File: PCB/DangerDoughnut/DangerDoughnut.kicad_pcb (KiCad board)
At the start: 4 copper layers, 50 x 37 mm, 85 parts, among them J1 Conn_01x02_Pin, J2 Conn_01x02_Pin, J3 Conn_01x02_Pin, J4 Conn_01x04_Pin, J6 USB_C_Receptacle_USB2.0_16P, U1 MMC5983MA, U10 ESP32-S3, U2 H3LIS331DLTR, U3 H3LIS331DLTR, U4 W25X20CLZP, U6 L5973D, U7 MIC5219-3.3YM5, U8 ESP8285H16, U9 SX1280IMLTRT, Y1 40MHz, Y2 52MHz, Y3 26MHz

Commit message: verified elsr
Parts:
- removed the C16 at (92.8, 70.2)
- removed the C17 at (88.8, 70.2)
- removed FL2: 2450FM07D0034T, Danger_Doughnut_Lib:FIL_2450FM07D0034T
- added C29: 100uF, Capacitor_THT:CP_Radial_D6.3mm_P2.50mm, B.Cu at (109.2, 59.5)
- added D6: Green LED, LED_SMD:LED_0805_2012Metric, F.Cu at (78.5, 64.8)
- added R20: 30, Resistor_SMD:R_0402_1005Metric, F.Cu at (78.5, 62.8)
- added R21: 100, Resistor_SMD:R_0402_1005Metric, F.Cu at (84.8, 56.8)
- added R22: 100, Resistor_SMD:R_0402_1005Metric, F.Cu at (86.6, 58.8)
- C1, C11, C14, C16, C17, C2, C20, C21, C22, C23, C25, C26, C27, C28, C3, C30, C32, C33, C6, C7, C9: footprint Capacitor_SMD:C_0603_1608Metric_Pad1.08x0.95mm_HandSolder -> Capacitor_SMD:C_0402_1005Metric
- C8: footprint Capacitor_SMD:CP_Elec_6.3x7.7 -> Capacitor_THT:CP_Radial_D6.3mm_P2.50mm
- D2: footprint Diode_SMD:D_SOD-882D -> Diode_SMD:D_0805_2012Metric
- D3: footprint Diode_SMD:D_SOD-882D -> Capacitor_SMD:C_0805_2012Metric
- R1, R10, R11, R12, R13, R14, R15, R16, R17, R18, R19, R2, R3, R4, R5, R6, R7, R8, R9: footprint Resistor_SMD:R_0603_1608Metric_Pad0.98x0.95mm_HandSolder -> Resistor_SMD:R_0402_1005Metric
- moved R16 4.56 mm to (100.0, 61.0), turned to -90 degrees
- moved C24 2.74 mm to (102.2, 70.0), turned to -90 degrees
- moved C23 2.25 mm to (100.5, 70.2)
- moved R12 2.00 mm to (99.0, 70.2)
- moved R17 1.68 mm to (101.8, 63.5)
- moved C26 1.66 mm to (101.8, 65.0)
- moved Y2 1.52 mm to (89.2, 70.5)
- moved C8 1.50 mm to (104.0, 66.5), turned to 180 degrees
- moved C15 1.35 mm to (97.8, 70.2)
- moved C5 1.35 mm to (93.8, 70.2)
- moved Y3 1.35 mm to (95.8, 70.2)
- moved D2 1.25 mm to (101.8, 45.5)
- moved U8 1.25 mm to (97.0, 65.5)
- moved D5 1.06 mm to (102.0, 61.0)
- moved kibuzzard-668D7854 1.06 mm to (106.0, 61.0)
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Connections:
- ANT2 pad 2: Net-(ANT2-FEED) -> unconnected-(ANT2-FEED-Pad2)
- J4 pad 1: GND -> Net-(J4-Pin_1)
- J4 pad 2: +5V -> Net-(J4-Pin_2)
- J4 pad 3: unconnected-(J4-Pin_3-Pad3) -> +5V
- J4 pad 4: unconnected-(J4-Pin_4-Pad4) -> GND
- U10 pad 1: Net-(U10-LNA_IN) -> unconnected-(U10-LNA_IN-Pad1)

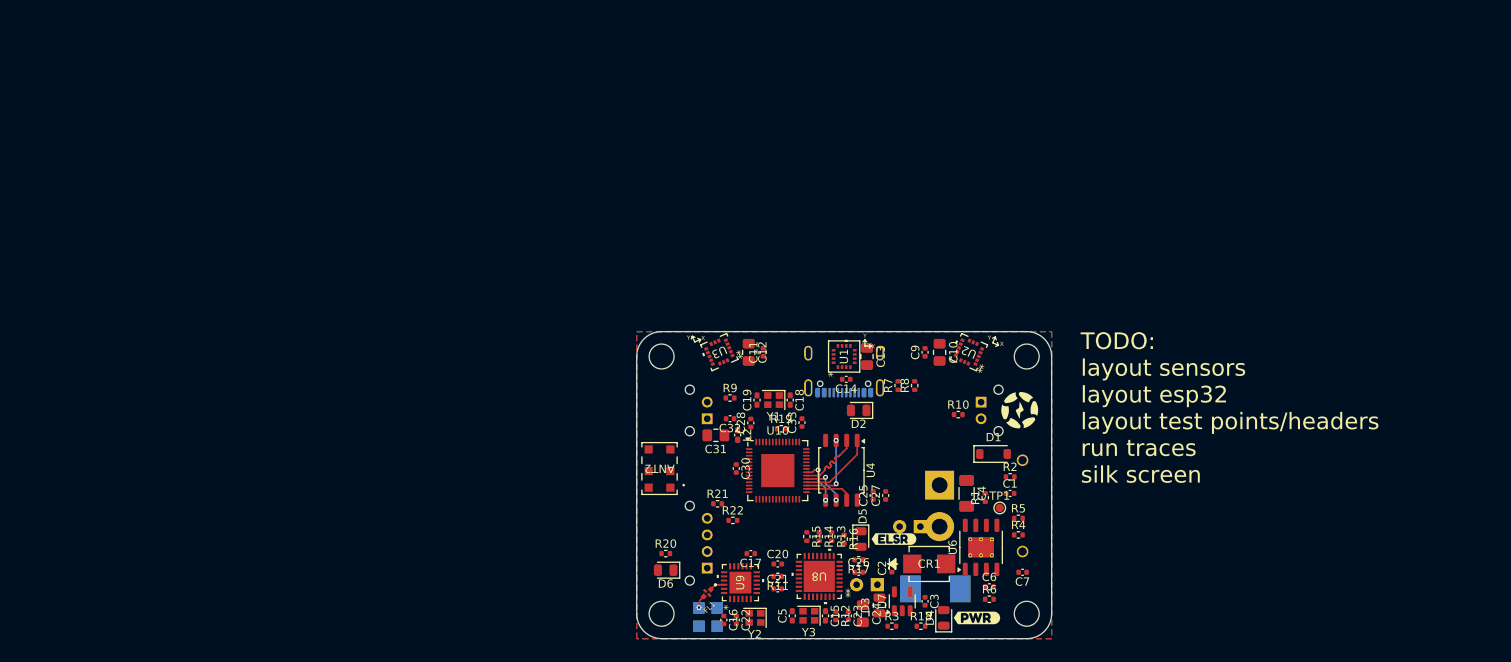
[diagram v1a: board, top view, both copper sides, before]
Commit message: updated schematic power layout done
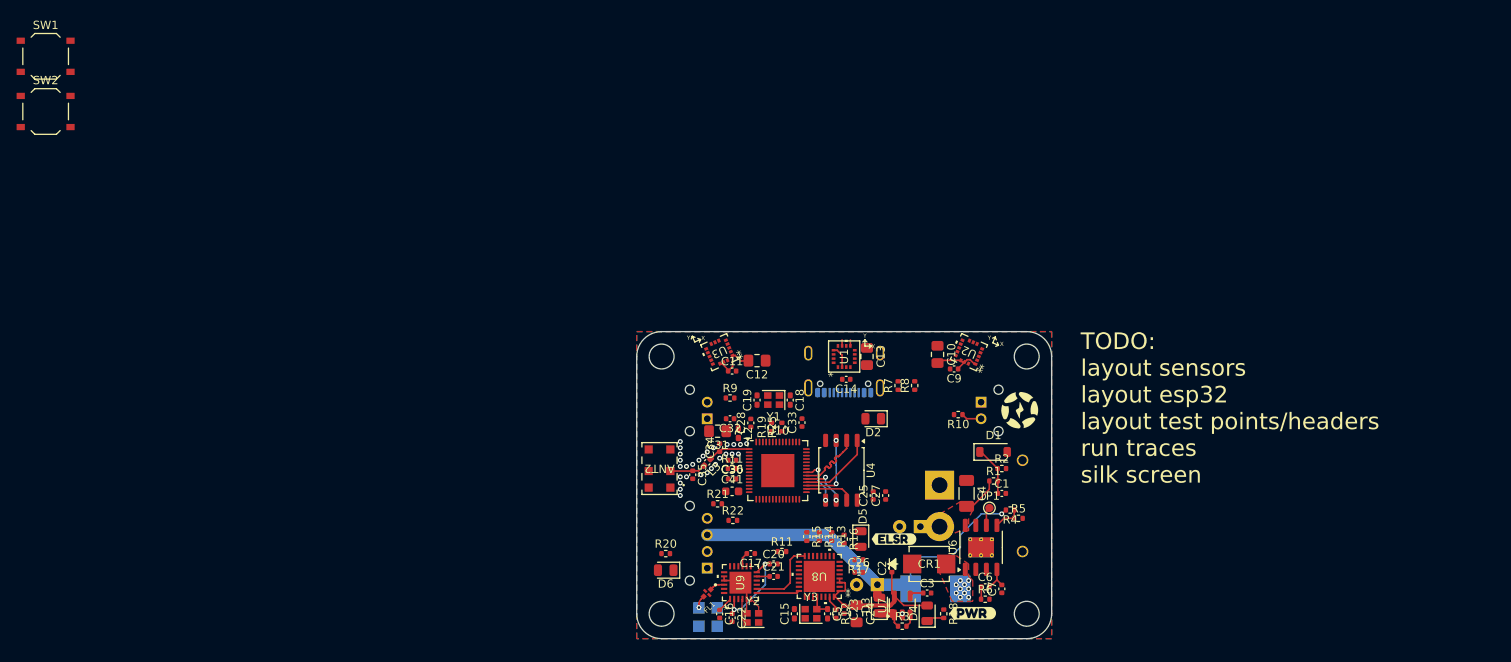
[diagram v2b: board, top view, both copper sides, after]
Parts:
- added C34: 1.8pF, Capacitor_SMD:C_0402_1005Metric, F.Cu at (85.0, 50.0)
- added C35: 1.2pF, Capacitor_SMD:C_0402_1005Metric, F.Cu at (81.8, 53.2)
- added C36: 1uF, Capacitor_SMD:C_0402_1005Metric, F.Cu at (86.5, 53.8)
- added C41: 100nF, Capacitor_SMD:C_0603_1608Metric, F.Cu at (86.5, 55.2)
- added L3: 3nH, Inductor_SMD:L_0402_1005Metric_Pad0.77x0.64mm_HandSolder, F.Cu at (83.5, 51.8)
- added R11: 10K, Resistor_SMD:R_0402_1005Metric, F.Cu at (86.5, 52.5)
- added R25: 510, Resistor_SMD:R_0402_1005Metric, F.Cu at (92.5, 47.5)
- added SW1: SW_Push, Button_Switch_SMD:SW_Push_1P1T_XKB_TS-1187A, F.Cu at (3.77, 2.83)
- added SW2: SW_Push, Button_Switch_SMD:SW_Push_1P1T_XKB_TS-1187A, F.Cu at (3.77, 9.47)
- D3: footprint Capacitor_SMD:C_0805_2012Metric -> Diode_SMD:D_0805_2012Metric
- R17, R18: value 2.2K -> 3.3k
- moved C11 4.37 mm to (86.5, 40.8), turned to 0 degrees
- moved C5 4.26 mm to (98.0, 70.0), turned to -90 degrees
- moved C9 4.03 mm to (113.2, 40.5), turned to 180 degrees
- moved C15 3.76 mm to (94.0, 70.0), turned to 90 degrees
- moved C7 3.20 mm to (119.0, 67.0), turned to 90 degrees
- moved R4 3.16 mm to (120.0, 57.5), turned to 180 degrees
- moved R18 3.13 mm to (112.0, 70.0), turned to -90 degrees
- moved R11 3.04 mm to (92.5, 62.5), turned to 0 degrees
- moved R1 2.24 mm to (118.0, 54.0), turned to 0 degrees
- moved D4 2.08 mm to (110.0, 69.9)
- moved D2 2.02 mm to (103.5, 46.5)
- moved C21 1.58 mm to (91.5, 65.5)
- moved C12 1.41 mm to (89.5, 39.5), turned to 180 degrees
- moved R2 1.41 mm to (119.0, 52.5)
- moved R3 1.25 mm to (107.0, 71.5)
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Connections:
- net Net-(U6-OUT) renamed /DCDC_OUT
- ANT2 pad 2: unconnected-(ANT2-FEED-Pad2) -> Net-(ANT2-FEED)
- C21 pad 1: Net-(U9-VBAT_IO) -> +3.3V
- U1 pad 15: unconnected-(U1-INT-Pad15) -> MAG_INT
- U10 pad 1: unconnected-(U10-LNA_IN-Pad1) -> Net-(U10-LNA_IN)
- U10 pad 10: unconnected-(U10-GPIO5-Pad10) -> Mag_CS
- U10 pad 11: unconnected-(U10-GPIO6-Pad11) -> Accel1_CS
- U10 pad 12: unconnected-(U10-GPIO7-Pad12) -> Accel2_CS
- U10 pad 16: unconnected-(U10-GPIO11-Pad16) -> LED_BOTTOM
- U10 pad 4: unconnected-(U10-CHIP_PU-Pad4) -> /ESP_RST
- U10 pad 49: unconnected-(U10-U0TXD-Pad49) -> Net-(U10-U0TXD)
- U10 pad 5: unconnected-(U10-GPIO0-Pad5) -> Net-(U10-GPIO0)
- U10 pad 50: unconnected-(U10-U0RXD-Pad50) -> ELSR_TX
- U10 pad 7: unconnected-(U10-GPIO2-Pad7) -> ACCEL2_INT
- U10 pad 8: unconnected-(U10-GPIO3-Pad8) -> ACCEL1_INT
- U10 pad 9: unconnected-(U10-GPIO4-Pad9) -> MAG_INT
- U2 pad 11: unconnected-(U2-INT1-Pad11) -> ACCEL1_INT
- U3 pad 11: unconnected-(U3-INT1-Pad11) -> ACCEL2_INT
- U9 pad 11: Net-(U9-VBAT_IO) -> +3.3V
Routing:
- net +5V: track 0.00 -> 46.7 mm, vias 0 -> 1
- net +3.3V: track 0.00 -> 37.8 mm
- net /DCC_FB: track 0.00 -> 11.4 mm, vias 0 -> 2
- net DIO1: track 0.00 -> 9.05 mm
- net GND: track 0.00 -> 8.05 mm, vias 0 -> 29
- net BATT: track 0.00 -> 5.98 mm
- net BUSY: track 0.00 -> 5.19 mm
- net Net-(U10-LNA_IN): track 0.00 -> 5.14 mm
- net +BATT: track 0.00 -> 4.60 mm
- net Net-(ANT2-FEED): track 0.00 -> 4.31 mm
- net /FB: track 0.00 -> 3.45 mm
- net Net-(U6-COMP): track 0.00 -> 3.38 mm
- net /MIC_IN: track 0.00 -> 3.37 mm
- net Net-(U9-XTA): track 0.00 -> 3.26 mm
- net Net-(U8-XTAL_IN): track 0.00 -> 2.83 mm
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- added copper zone on F.Cu, net +BATT
- added copper zone on F.Cu, net /DCDC_OUT

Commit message: updated layout
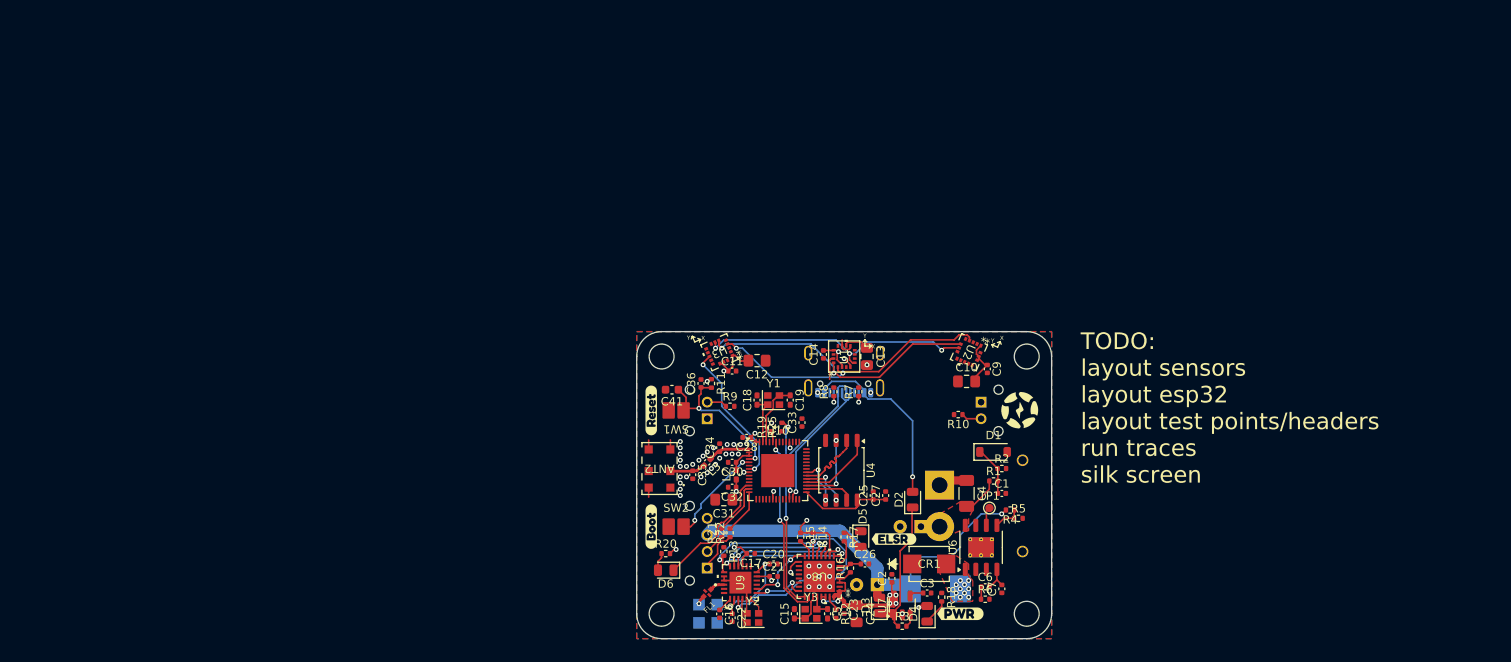
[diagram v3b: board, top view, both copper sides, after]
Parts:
- removed the R11 at (92.5, 62.5)
- added kibuzzard-66EFAD11: G***, kibuzzard-66EFAD11, F.Cu at (76.8, 45.5)
- added kibuzzard-66EFAD22: G***, kibuzzard-66EFAD22, F.Cu at (76.8, 59.5)
- C29: footprint Capacitor_THT:CP_Radial_D6.3mm_P2.50mm -> Danger_Doughnut_Lib:CP_Right_Angle_D6.3_P2.50_H16.5
- SW1, SW2: footprint Button_Switch_SMD:SW_Push_1P1T_XKB_TS-1187A -> Danger_Doughnut_Lib:Pad_Button
- moved SW2 91.0 mm to (79.8, 59.5)
- moved SW1 87.1 mm to (79.8, 45.5), turned to 180 degrees
- moved C41 14.2 mm to (79.2, 43.0), turned to 180 degrees
- moved R13 13.1 mm to (85.5, 62.5)
- moved C36 12.1 mm to (82.8, 42.2), turned to 90 degrees
- moved D2 10.8 mm to (108.2, 56.2), turned to 90 degrees
- moved R11 10.6 mm to (84.0, 42.2), turned to -90 degrees
- moved R8 9.78 mm to (98.8, 43.2)
- moved C31 8.28 mm to (85.5, 56.2)
- moved C32 8.25 mm to (86.5, 54.8)
- moved L2 5.01 mm to (87.0, 53.2), turned to 90 degrees
- moved R7 4.81 mm to (101.8, 43.2)
- moved C10 4.78 mm to (114.8, 42.0), turned to 0 degrees
- moved C14 4.07 mm to (97.5, 38.8), turned to 90 degrees
- moved C18 4.00 mm to (89.5, 44.2), turned to 90 degrees
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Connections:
- C41 pad 2: Net-(C41-Pad2) -> GND
- SW1 pad 2: Net-(C41-Pad2) -> GND
- U10 pad 12: Accel2_CS -> LED_BOTTOM
- U10 pad 14: ESC_L -> LED_SCK
- U10 pad 16: LED_BOTTOM -> unconnected-(U10-GPIO11-Pad16)
- U10 pad 24: LED_SCK -> unconnected-(U10-GPIO18-Pad24)
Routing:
- net MOSI_2: track 0.00 -> 34.9 mm, vias 0 -> 2
- net SCK_2: track 0.00 -> 34.6 mm, vias 0 -> 2
- net MISO_2: track 0.00 -> 33.8 mm, vias 0 -> 3
- net +3.3V: track 37.8 -> 65.9 mm, vias 0 -> 20
- net N_RST: track 0.00 -> 24.6 mm, vias 0 -> 2
- net ELSR_RX: track 0.00 -> 23.1 mm, vias 0 -> 2
- net Net-(D2-A): track 0.00 -> 22.4 mm, vias 0 -> 1
- net ELSR_TX: track 0.00 -> 22.2 mm, vias 0 -> 2
- net /ESP_RST: track 0.00 -> 19.3 mm, vias 0 -> 2
- net SX_CS: track 0.00 -> 17.8 mm, vias 0 -> 2
- net D-: track 0.00 -> 17.6 mm, vias 0 -> 1
- net ACCEL2_INT: track 0.00 -> 17.6 mm, vias 0 -> 2
- net D+: track 0.00 -> 17.0 mm, vias 0 -> 1
- net SX_SCK: track 0.00 -> 16.1 mm, vias 0 -> 2
- net SX_MISO: track 0.00 -> 15.2 mm, vias 0 -> 2
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- added copper zone on B.Cu, net +3.3V
- removed copper zone on B.Cu, net GND

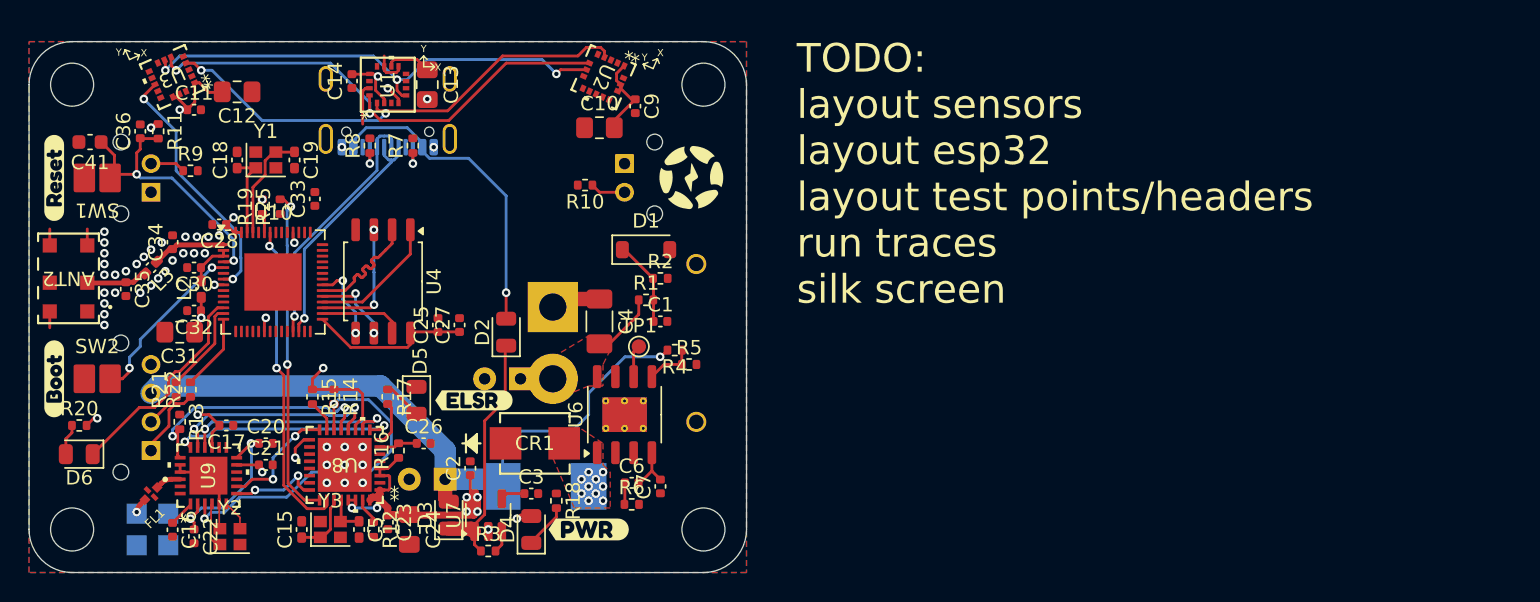
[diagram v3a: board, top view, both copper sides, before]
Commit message: updated layout needs 3v3 headers testpoints and verify
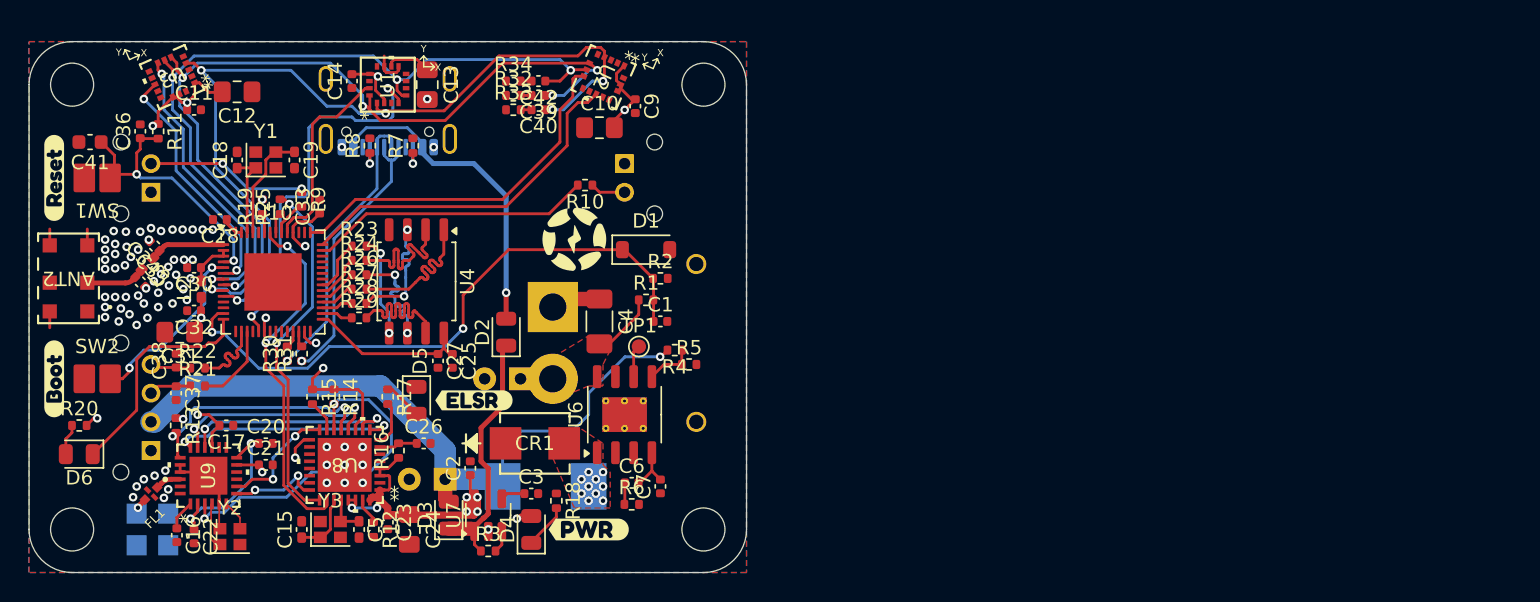
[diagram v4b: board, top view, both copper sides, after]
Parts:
- added C37: C, Capacitor_SMD:C_0402_1005Metric, F.Cu at (85.2, 60.5)
- added C38: C, Capacitor_SMD:C_0402_1005Metric, F.Cu at (85.2, 58.2)
- added C39: 100pF, Capacitor_SMD:C_0402_1005Metric, F.Cu at (110.5, 39.8)
- added C40: 100pF, Capacitor_SMD:C_0402_1005Metric, F.Cu at (110.5, 40.8)
- added C42: 100pF, Capacitor_SMD:C_0402_1005Metric, F.Cu at (110.5, 38.8)
- added R23: 0, Resistor_SMD:R_0402_1005Metric, F.Cu at (98.0, 50.2)
- added R24: 0, Resistor_SMD:R_0402_1005Metric, F.Cu at (98.0, 51.2)
- added R26: 0, Resistor_SMD:R_0402_1005Metric, F.Cu at (98.0, 52.2)
- added R27: 0, Resistor_SMD:R_0402_1005Metric, F.Cu at (98.0, 53.2)
- added R28: 0, Resistor_SMD:R_0402_1005Metric, F.Cu at (98.0, 54.2)
- added R29: 0, Resistor_SMD:R_0402_1005Metric, F.Cu at (98.0, 55.2)
- added R30: 0, Resistor_SMD:R_0402_1005Metric, F.Cu at (93.0, 57.8)
- added R31: 0, Resistor_SMD:R_0402_1005Metric, F.Cu at (94.0, 57.8)
- added R32: 100, Resistor_SMD:R_0402_1005Metric, F.Cu at (108.8, 39.8)
- added R33: 100, Resistor_SMD:R_0402_1005Metric, F.Cu at (108.8, 40.8)
- added R34: 100, Resistor_SMD:R_0402_1005Metric, F.Cu at (108.8, 38.8)
- R21, R22: value 100 -> 33
- moved R9 8.00 mm to (94.0, 47.0), turned to -90 degrees
- moved C27 2.92 mm to (103.5, 58.2), turned to -90 degrees
- moved C25 2.69 mm to (104.5, 58.2), turned to -90 degrees
- moved U4 2.33 mm to (102.0, 52.7)
- moved R22 1.58 mm to (86.8, 58.8), turned to 0 degrees
- moved R21 1.52 mm to (86.8, 60.0), turned to 0 degrees
- moved C34 1.28 mm to (83.8, 50.2), turned to 135 degrees
- moved C35 1.12 mm to (82.8, 52.8), turned to -45 degrees
- moved C33 0.63 mm to (95.2, 47.5)
- moved C16 0.48 mm to (85.3, 70.4)
- moved C28 0.35 mm to (88.3, 48.4)
- moved L3 0.35 mm to (83.2, 51.5)
- moved R13 0.35 mm to (85.2, 62.8)
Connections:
- J4 pad 1: Net-(J4-Pin_1) -> GND
- J4 pad 2: Net-(J4-Pin_2) -> +5V
- J4 pad 3: +5V -> Net-(J4-Pin_3)
- J4 pad 4: GND -> Net-(J4-Pin_4)
- R21 pad 1: Net-(J4-Pin_2) -> Net-(J4-Pin_3)
- R21 pad 2: LED_MOSI -> LED_SCK
- R22 pad 1: Net-(J4-Pin_1) -> Net-(J4-Pin_4)
- R22 pad 2: LED_SCK -> LED_MOSI
- U10 pad 10: Mag_CS -> SCK_2
- U10 pad 11: Accel1_CS -> unconnected-(U10-GPIO6-Pad11)
- U10 pad 12: LED_BOTTOM -> unconnected-(U10-GPIO7-Pad12)
- U10 pad 13: LED_MOSI -> BATT
- U10 pad 14: LED_SCK -> LED_BOTTOM
- U10 pad 15: ESC_R -> unconnected-(U10-GPIO10-Pad15)
- U10 pad 16: unconnected-(U10-GPIO11-Pad16) -> LED_MOSI
- U10 pad 17: BATT -> LED_SCK
- U10 pad 18: SCK_2 -> unconnected-(U10-GPIO13-Pad18)
- U10 pad 19: MOSI_2 -> Mag_CS
- U10 pad 25: D- -> Net-(U10-GPIO19/USB_D-)
- U10 pad 26: D+ -> Net-(U10-GPIO20/USB_D+)
- U10 pad 27: MISO_2 -> unconnected-(U10-GPIO21-Pad27)
- U10 pad 30: SPIHD -> Net-(U10-SPIHD)
- U10 pad 31: SPIWP -> Net-(U10-SPIWP)
- U10 pad 32: SPICS0 -> Net-(U10-SPICS0)
- U10 pad 33: SPICLK -> Net-(U10-SPICLK)
- U10 pad 34: SPIQ -> Net-(U10-SPIQ)
- U10 pad 35: SPID -> Net-(U10-SPID)
- U10 pad 41: unconnected-(U10-GPIO36-Pad41) -> ESC_R
- U10 pad 42: unconnected-(U10-GPIO37-Pad42) -> ACCEL1_INT
- U10 pad 43: unconnected-(U10-GPIO38-Pad43) -> Accel1_CS
- U10 pad 47: unconnected-(U10-MTDI-Pad47) -> MAG_INT
- U10 pad 48: unconnected-(U10-MTMS-Pad48) -> ESC_L
- U10 pad 6: unconnected-(U10-GPIO1-Pad6) -> ACCEL2_INT
- U10 pad 7: ACCEL2_INT -> Accel2_CS
- U10 pad 8: ACCEL1_INT -> MISO_2
- U10 pad 9: MAG_INT -> MOSI_2
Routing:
- net BATT: track 5.98 -> 42.3 mm, vias 0 -> 2
- net SCK_2: track 34.6 -> 61.5 mm, vias 2 -> 5
- net MOSI_2: track 34.9 -> 61.5 mm, vias 2 -> 5
- net Accel1_CS: track 0.00 -> 25.6 mm
- net Mag_CS: track 1.34 -> 26.6 mm, vias 1 -> 2
- net ACCEL1_INT: track 0.63 -> 24.7 mm, vias 1 -> 0
- net MISO_2: track 33.8 -> 54.6 mm, vias 3 -> 4
- net Accel2_CS: track 0.00 -> 20.5 mm, vias 0 -> 2
- net ESC_R: track 0.00 -> 19.7 mm
- net MAG_INT: track 2.86 -> 13.8 mm
- net Net-(J3-Pin_2): track 2.45 -> 11.2 mm, vias 0 -> 2
- net SPIHD: track 5.88 -> 11.4 mm
- net Net-(J4-Pin_1): track 5.22 -> 0.00 mm
- net +3.3V: track 65.9 -> 70.3 mm
- net Net-(U10-SPID): track 0.00 -> 3.75 mm
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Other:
- board text added: "TODO: layout sensors layout esp32 layout test points/headers run traces silk screen flip LED wiring"
- board text removed: "TODO: layout sensors layout esp32 layout test points/headers run traces silk screen"
